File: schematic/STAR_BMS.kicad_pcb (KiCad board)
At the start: 2 copper layers, 112 parts, among them J1 694106301002, J10 B3B-XH-A_LF__SN_, J11 1017491, J12 B3B-XH-A_LF__SN_, J13 1017491, J2 External Thermistor (MF52C110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, J3 External Thermistor (MF52C110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, J4 External Thermistor (MF52C110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, J5 External Thermistor (MF52C110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, J6 External Thermistor (MF52C110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, J7 6120XX21621_61200621621, J8 SMB, J9 1017491, Q1 SSM6J507NU-LF, Q2 TPHR6503PL1-LQ, Q3 TPHR6503PL1-LQ, Q4 DMN3042L-7, Q5 TPHR6503PL1-LQ, Q6 FDN358P, Q7 TPHR6503PL1-LQ, Q8 2N7002K, U1 BQ24600RVAT, U2 BQ4050RSMR, U3 BQ296103DSGR

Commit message: current state
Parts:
- added D13: YG, SML-D12Y1WT86:LEDC1608X55N, F.Cu at (106.0, 248.5)
- added D14: YG, SML-D12Y1WT86:LEDC1608X55N, F.Cu at (103.3, 248.6)
- added R43: 10k, Resistor_SMD:R_0603_1608Metric_Pad0.98x0.95mm_HandSolder, F.Cu at (106.0, 244.2)
- added R44: 10k, Resistor_SMD:R_0603_1608Metric_Pad0.98x0.95mm_HandSolder, F.Cu at (103.2, 244.2)
- moved C7 202.4 mm to (100.8, 244.0), turned to -90 degrees
- moved C8 200.9 mm to (97.8, 244.0), turned to -90 degrees
- moved C12 194.2 mm to (155.1, 257.8)
- moved C13 194.2 mm to (155.1, 260.8)
- moved C14 194.2 mm to (155.1, 263.8)
- moved J1 175.3 mm to (60.9, 245.1)
- moved C11 175.0 mm to (161.9, 273.4)
- moved C3 175.0 mm to (161.9, 258.3)
- moved C4 175.0 mm to (161.9, 260.8)
- moved C5 175.0 mm to (161.9, 263.3)
- moved C6 175.0 mm to (161.9, 265.8)
- moved C9 175.0 mm to (161.9, 268.3)
- moved C10 175.0 mm to (161.9, 270.8)
- moved C1 174.6 mm to (87.3, 249.1)
- moved R1 172.0 mm to (86.0, 245.8), turned to -90 degrees
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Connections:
- C3 pad 2: C_GND -> CH_GND
- C4 pad 2: C_GND -> CH_GND
- C5 pad 2: C_GND -> CH_GND
- C7 pad 2: C_GND -> CH_GND
- C8 pad 2: C_GND -> CH_GND
- J2 pad 2: C_GND -> CH_GND
- R5 pad 2: C_GND -> CH_GND
- R8 pad 2: C_GND -> CH_GND
- U1 pad 3: unconnected-(U1-STAT-Pad3) -> Net-(U1-STAT)
- U1 pad 5: unconnected-(U1-~{PG}-Pad5) -> Net-(U1-~{PG})

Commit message: update for now
update for now
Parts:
- R9: footprint Resistor_SMD:R_0603_1608Metric_Pad0.98x0.95mm_HandSolder -> LVK12R010FER:RESCAF_LVK12-4
- moved J2 222.1 mm to (36.2, 82.5)
- moved C9 214.4 mm to (74.3, 72.7)
- moved C11 212.5 mm to (79.4, 77.5), turned to -90 degrees
- moved Q7 208.5 mm to (116.8, 80.2), turned to 180 degrees
- moved C10 202.4 mm to (92.1, 80.9), turned to -90 degrees
- moved C3 198.6 mm to (71.8, 81.3), turned to 90 degrees
- moved C6 196.5 mm to (86.4, 84.5), turned to 90 degrees
- moved C14 196.2 mm to (106.0, 73.9), turned to 90 degrees
- moved Q5 195.8 mm to (116.8, 90.1)
- moved R37 194.9 mm to (111.1, 84.5), turned to -90 degrees
- moved C13 194.2 mm to (102.2, 73.9), turned to 90 degrees
- moved U2 192.6 mm to (103.1, 100.3)
- moved S1 192.5 mm to (109.9, 79.4), turned to -90 degrees
- moved C12 192.4 mm to (98.4, 73.9), turned to 90 degrees
- moved C5 189.9 mm to (82.5, 90.8), turned to -90 degrees
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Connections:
- net Net-(U1-PH) renamed /PH PIN
- C10 pad 1: Net-(U1-SRP) -> Net-(R9-V_2)
- C11 pad 1: Net-(U1-SRP) -> Net-(R9-V_2)
- C11 pad 2: /PACK+ -> Net-(R9-V_1)
- C25 pad 2: Net-(Q8-S) -> /PACK+
- L1 pad 2: Net-(U1-SRP) -> Net-(R9-I_2)
- Q7 pad 1: Net-(Q8-S) -> /PACK+
- Q7 pad 2: Net-(Q8-S) -> /PACK+
- Q7 pad 3: Net-(Q8-S) -> /PACK+
- Q8 pad 2: Net-(Q8-S) -> /PACK+
- R34 pad 1: Net-(Q8-S) -> /PACK+
- R36 pad 1: Net-(Q8-S) -> /PACK+
- R9 pad 1: Net-(U1-SRP) -> Net-(R9-V_1)
- U1 pad 10: Net-(U1-SRP) -> Net-(R9-V_2)
- U1 pad 9: /PACK+ -> Net-(R9-V_1)

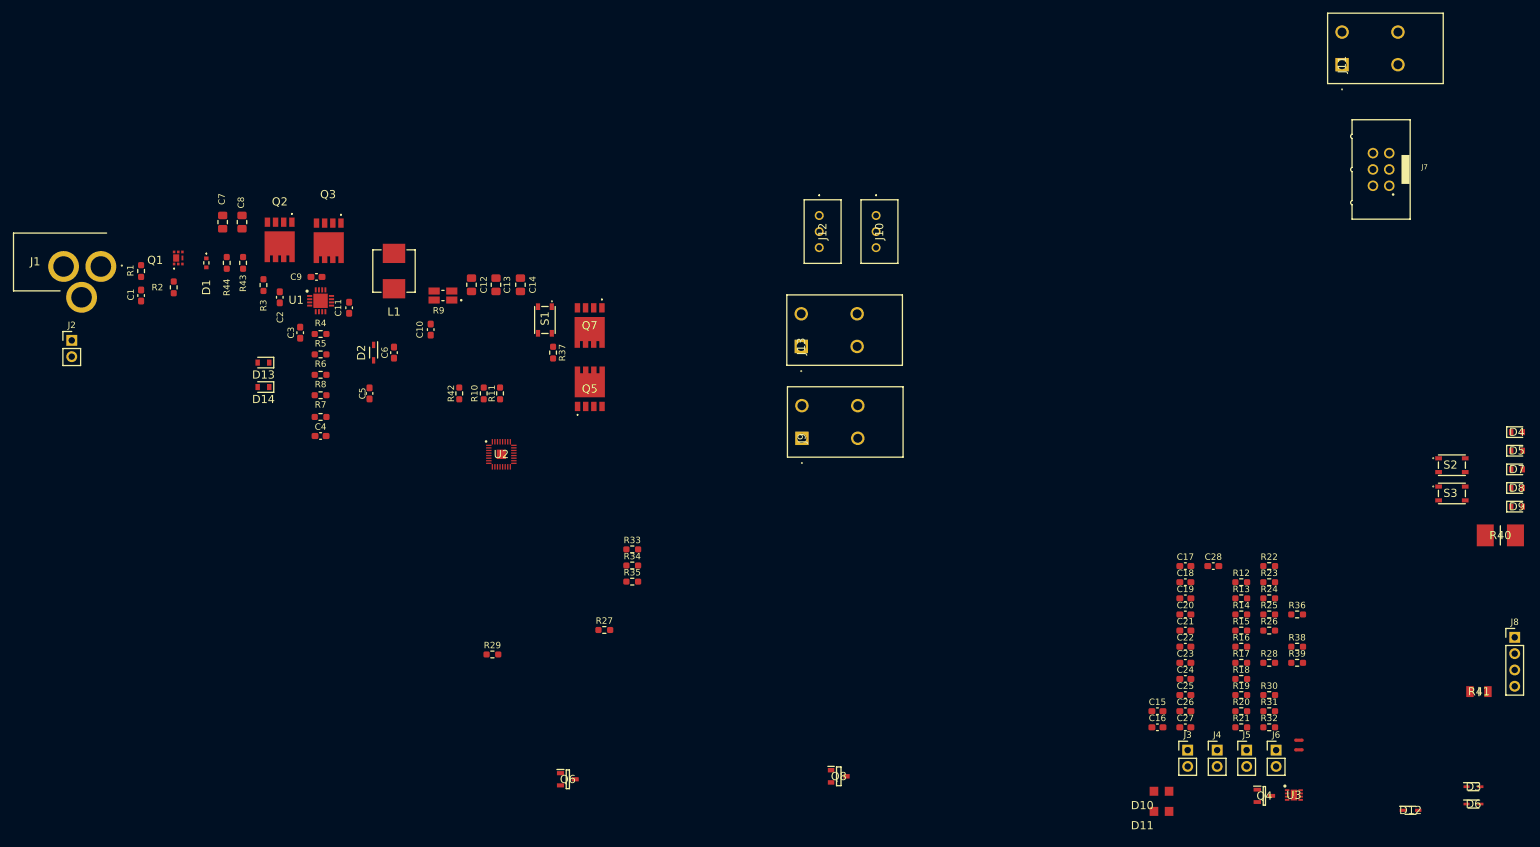
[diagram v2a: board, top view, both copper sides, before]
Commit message: Before Holes
Before Holes, leds, and the i2s/smb, bom, digital ground flood  plane layer 3, stich pours using via.
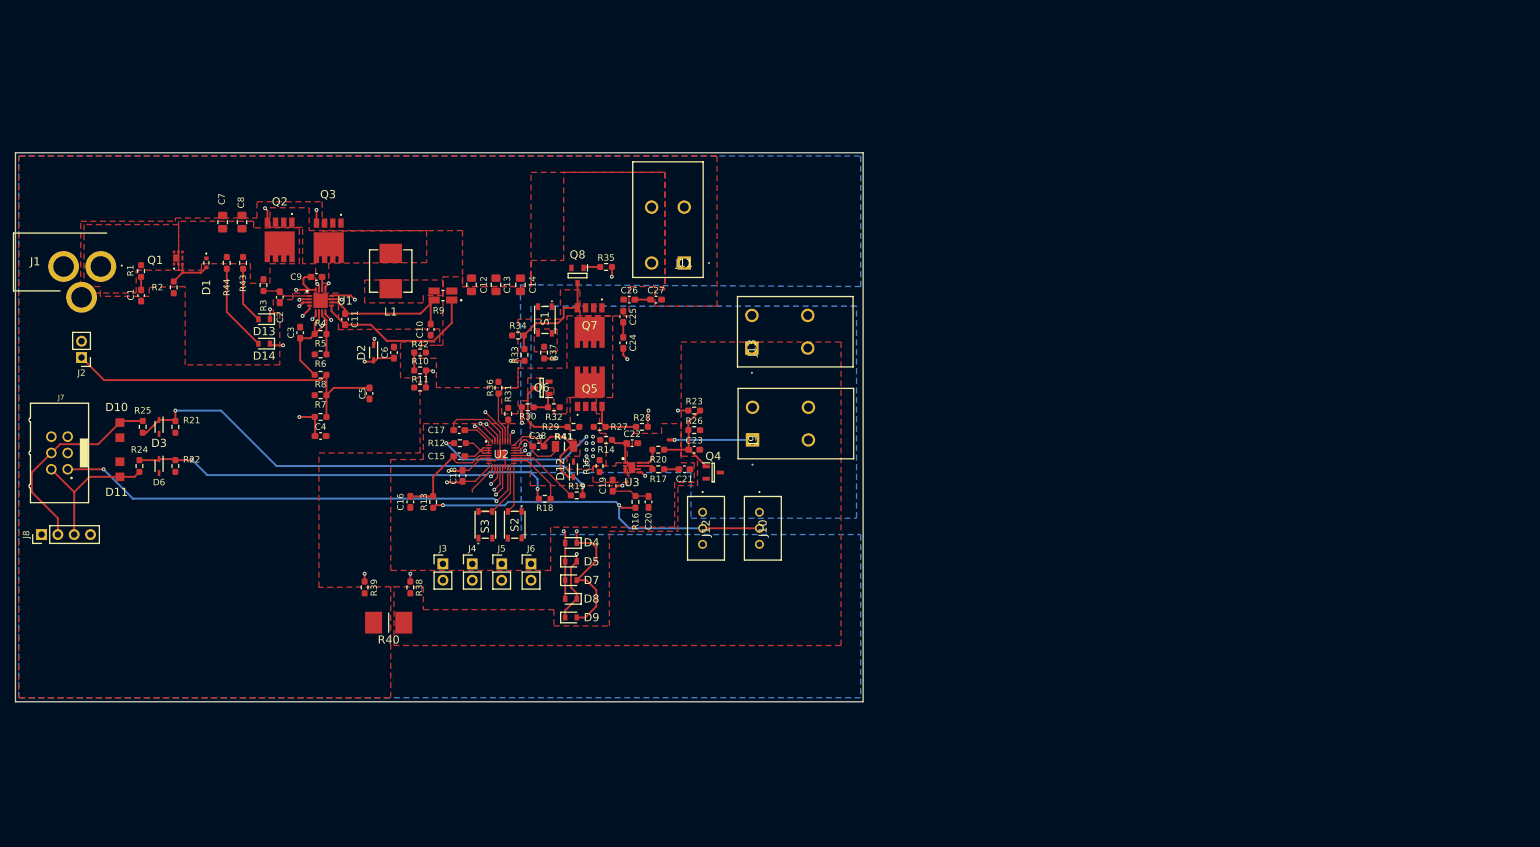
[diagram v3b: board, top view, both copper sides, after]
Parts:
- removed NT1: NetTie_2, NetTie:NetTie-2_SMD_Pad0.5mm
- moved J8 229.9 mm to (31.5, 112.8), turned to 90 degrees
- moved D3 212.2 mm to (49.8, 96.0), turned to -90 degrees
- moved D6 211.3 mm to (49.8, 102.1), turned to -90 degrees
- moved J7 210.4 mm to (34.3, 100.1)
- moved R25 177.8 mm to (47.2, 96.0), turned to 90 degrees
- moved R24 177.1 mm to (46.7, 102.1), turned to -90 degrees
- moved R40 173.6 mm to (85.5, 126.5), turned to 180 degrees
- moved R21 172.4 mm to (52.3, 96.0), turned to 90 degrees
- moved D10 171.6 mm to (43.7, 96.5), turned to 90 degrees
- moved R22 171.0 mm to (52.3, 102.1), turned to 90 degrees
- moved D11 170.7 mm to (43.7, 102.6), turned to -90 degrees
- moved S3 150.5 mm to (100.6, 111.3), turned to 90 degrees
- moved D4 148.3 mm to (113.9, 114.1), turned to 180 degrees
- moved D5 148.3 mm to (113.9, 117.0)
- moved D7 148.3 mm to (113.9, 119.9)
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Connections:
- J10 pad 3: GND -> AGND
- J11 pad 1: GND -> CH_GND
- J11 pad 2: GND -> CH_GND
- J12 pad 3: GND -> AGND
- J13 pad 1: GND -> AGND
- J13 pad 2: GND -> AGND
- J7 pad 3: GND -> CH_GND
- J7 pad 5: GND -> CH_GND
- J7 pad 6: GND -> CH_GND
- J9 pad 1: GND -> AGND
- J9 pad 2: GND -> AGND
- NT2 pad 1: AGND -> GND
- NT2 pad 2: GND -> AGND
- R38 pad 1: GND -> AGND
- R40 pad 1: CH_GND -> AGND
- R40 pad 2: GND -> CH_GND
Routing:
- net Net-(D3-K): track 0.00 -> 77.3 mm, vias 0 -> 2
- net /BTP_INT: track 0.00 -> 74.9 mm, vias 0 -> 2
- net Net-(D6-K): track 0.00 -> 67.0 mm, vias 0 -> 2
- net /CELL1_VP: track 0.00 -> 56.8 mm, vias 0 -> 2
- net Net-(J2-Pin_1): track 0.00 -> 53.7 mm
- net Net-(U2-LEDCNTLC): track 0.00 -> 46.7 mm, vias 0 -> 2
- net Net-(D12-K): track 0.00 -> 35.7 mm, vias 0 -> 2
- net Net-(U2-LEDCNTLB): track 0.00 -> 35.1 mm, vias 0 -> 2
- net Net-(U2-CHG): track 0.00 -> 33.9 mm, vias 0 -> 2
- net Net-(U2-LEDCNTLA): track 0.00 -> 32.4 mm, vias 0 -> 2
- net /BMS_SMBUS_CLK: track 0.00 -> 31.9 mm
- net Net-(U2-FUSE): track 0.00 -> 30.4 mm, vias 0 -> 2
- net Net-(U2-SRN): track 0.00 -> 29.8 mm, vias 0 -> 2
- net /CELL2_VP: track 0.00 -> 29.4 mm, vias 0 -> 12
- net Net-(R9-V_1): track 0.00 -> 26.2 mm
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- added copper zone on F.Cu, net /BARREL_IN
- added copper zone on B.Cu, net /CELL2_VP
- added copper zone on F.Cu, net /CELL2_VP
- added copper zone on F.Cu, net /PACK+
- added copper zone on F.Cu, net /PH PIN
- added copper zone on B.Cu, net AGND
- added copper zone on F.Cu, net AGND
- added copper zone on F.Cu, net CH_GND
- added copper zone on In1.Cu, net CH_GND
- added copper zone on F.Cu, net GND
- added copper zone on In2.Cu, net GND
- added copper zone on F.Cu, net Net-(J1-POWER)
- added copper zone on F.Cu, net Net-(Q6-S)
- added copper zone on F.Cu, net Net-(R37-Pad1)
- added copper zone on F.Cu, net Net-(R9-I_2)
- added copper zone on F.Cu, net Net-(U3-V2)
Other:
- board outline added: 132 x 85.5 mm
- copper layers 2 -> 4

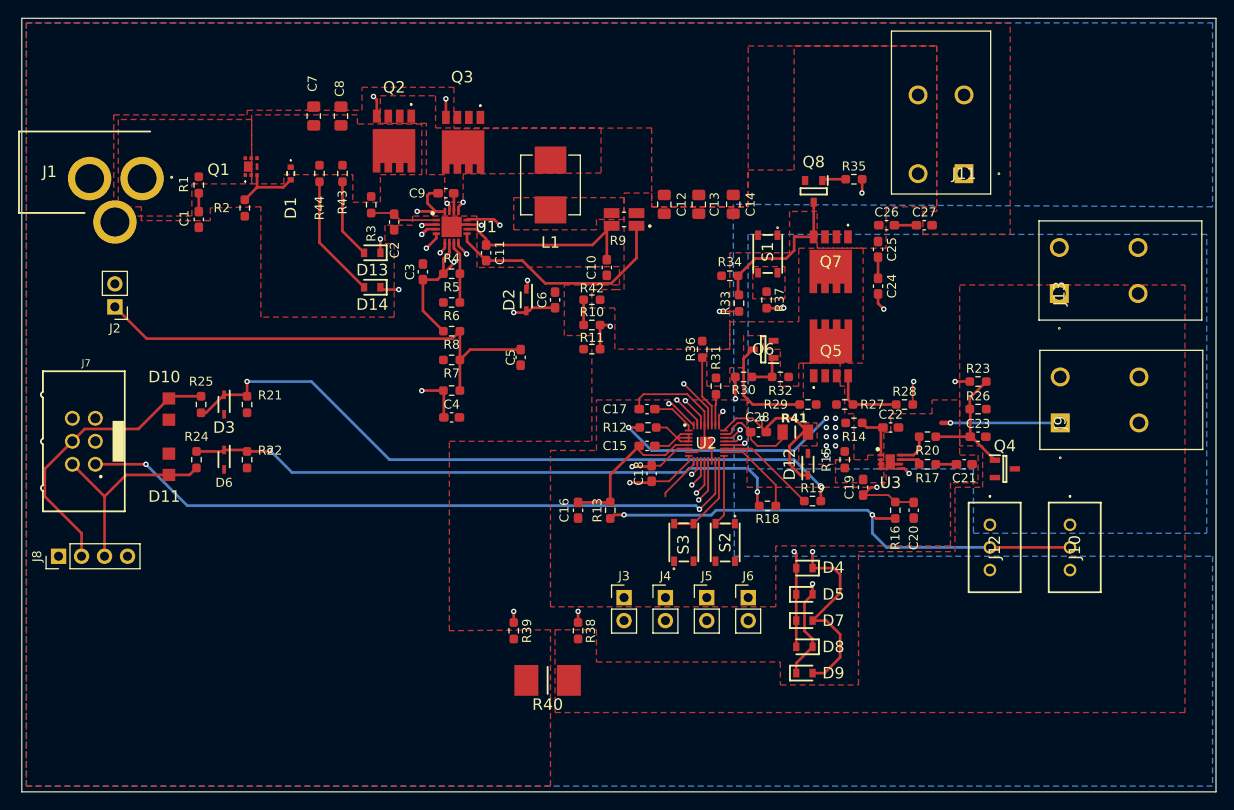
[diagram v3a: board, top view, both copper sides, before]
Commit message: BMS Completed basically
Only thing needed is an addition of the 90 degree header pins on the left side. LEDs, BOM, and stiching was completed
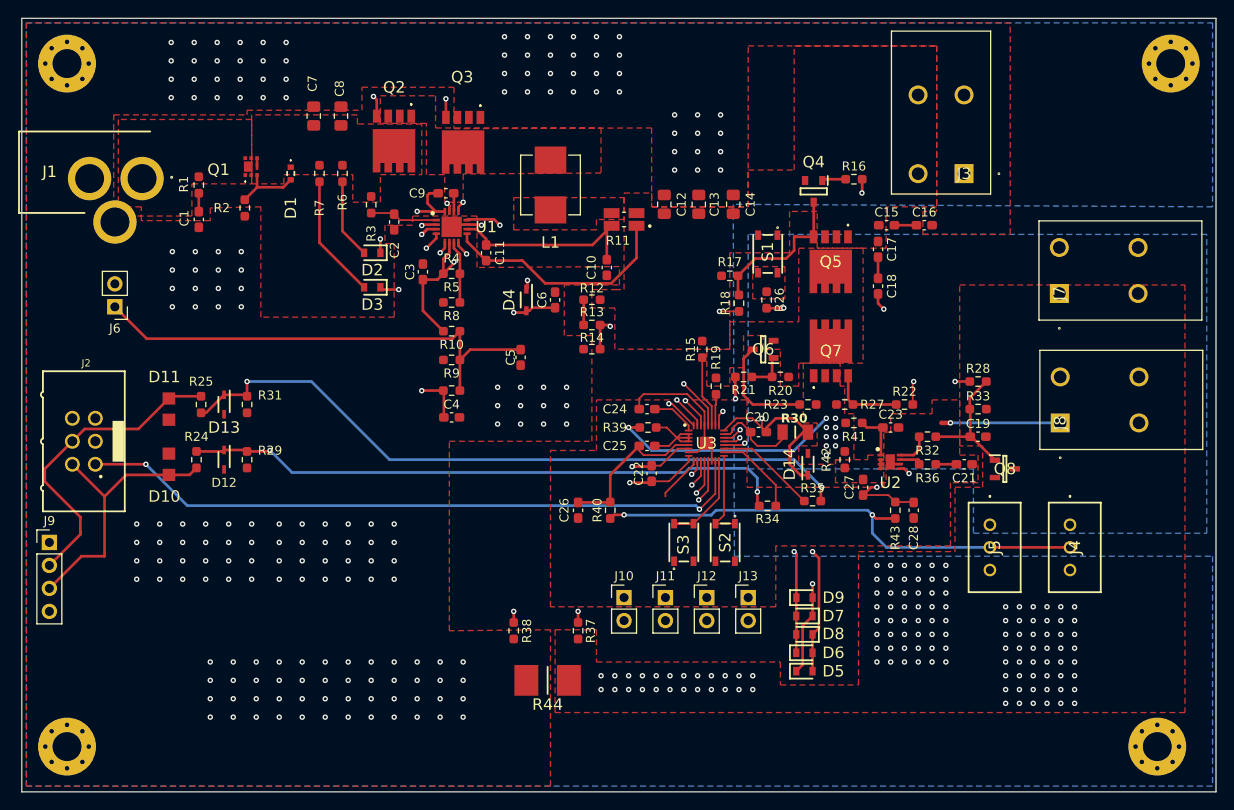
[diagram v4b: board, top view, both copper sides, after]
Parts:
- added H1: M3 Via, MountingHole:MountingHole_3.2mm_M3_Pad_Via, F.Cu at (32.4, 58.3)
- added H2: M3 Via, MountingHole:MountingHole_3.2mm_M3_Pad_Via, F.Cu at (152.9, 133.8)
- added H3: M3 Via, MountingHole:MountingHole_3.2mm_M3_Pad_Via, F.Cu at (32.4, 133.8)
- added H4: M3 Via, MountingHole:MountingHole_3.2mm_M3_Pad_Via, F.Cu at (154.4, 58.3)
- Q8: renamed from Q4; footprint DMN2004K-7:SOT96P240X115-3N -> DMN3042L-7:SOT96P240X115-3N
- moved D8 7.32 mm to (113.9, 121.4)
- moved D6 3.56 mm to (113.9, 123.4)
- moved D7 3.41 mm to (113.9, 119.4)
- moved J9 1.83 mm to (30.5, 111.3), turned to 0 degrees
- moved D9 0.36 mm to (113.9, 117.3)
- moved D5 0.21 mm to (113.9, 125.5)
- renumbered C26 to C15, C27 to C16, C25 to C17, C24 to C18, C23 to C19, C28 to C20, C18 to C22, C22 to C23, C17 to C24, C15 to C25, C16 to C26, C19 to C27, C20 to C28, D11 to D10, D10 to D11, D6 to D12, D3 to D13, D12 to D14, D13 to D2, D14 to D3, D2 to D4, D9 to D5, D7 to D6, D8 to D7, D4 to D8, D5 to D9, J3 to J10, J4 to J11, J5 to J12, J6 to J13, J7 to J2, J11 to J3, J10 to J4, J12 to J5, J2 to J6, J13 to J7, J9 to J8, J8 to J9, NT2 to NT1, Q8 to Q4, Q7 to Q5, Q5 to Q7, R8 to R10, R9 to R11, R42 to R12, R10 to R13, R11 to R14, R36 to R15, R35 to R16, R34 to R17, R33 to R18, R31 to R19, R32 to R20, R30 to R21, R28 to R22, R29 to R23, R37 to R26, R23 to R28, R22 to R29, R41 to R30, R21 to R31, R20 to R32, R26 to R33, R18 to R34, R19 to R35, R17 to R36, R38 to R37, R39 to R38, R12 to R39, R13 to R40, R14 to R41, R15 to R42, R16 to R43, R40 to R44, R43 to R6, R44 to R7, R6 to R8, R7 to R9, U3 to U2, U2 to U3
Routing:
- net Net-(U3-LEDCNTLC): track 46.7 -> 39.0 mm
- net /BMS_SMBUS_DATA: track 23.1 -> 30.7 mm
- net /BMS_SMBUS_CLK: track 31.9 -> 34.3 mm
- net Net-(U3-LEDCNTLA): track 32.4 -> 31.4 mm
- net /BARREL_IN: track 0.00 -> 0.94 mm
- net Net-(U3-LEDCNTLB): track 35.1 -> 35.8 mm
- net CH_GND: vias 2 -> 186
- net AGND: vias 1 -> 121
- removed copper zone on In2.Cu, net GND

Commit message: bms
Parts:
- J9: value SMB -> 22053041; footprint Connector_PinHeader_2.54mm:PinHeader_1x04_P2.54mm_Vertical -> 22053041:CONN_A-7478-04A_MOL
- moved J9 14.5 mm to (42.5, 119.4), turned to -90 degrees
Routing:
- net /BMS_SMBUS_CLK: track 34.3 -> 43.1 mm
- net /BMS_SMBUS_DATA: track 30.7 -> 35.7 mm
